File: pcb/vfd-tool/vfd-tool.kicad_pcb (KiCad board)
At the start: 2 copper layers, 167 parts, among them J1 Conn_ARM_SWD_TagConnect_TC203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, J2 USB_C_Receptacle_USB2.0, J3 Micro_SD_Card, J4 Conn_01x10, J5 Raspberry_Pi_2_3, J6 Conn_02x15_Odd_Even, J7 Conn_02x15_Odd_Even, J8 Conn_02x08_Odd_Even, J9 Conn_01x02_Socket, SW1 SW_Push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

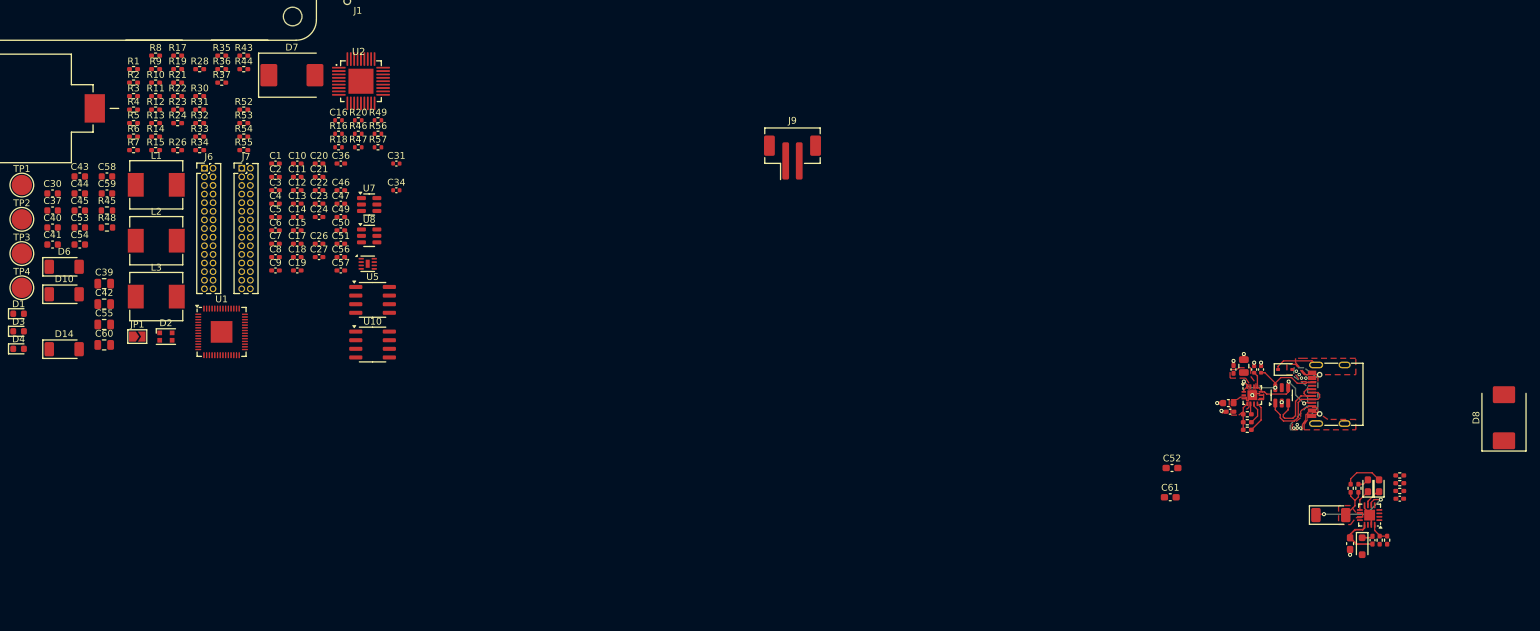
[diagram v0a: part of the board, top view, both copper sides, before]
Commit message: 3V3 + Charging + Fuel gauge PCB done
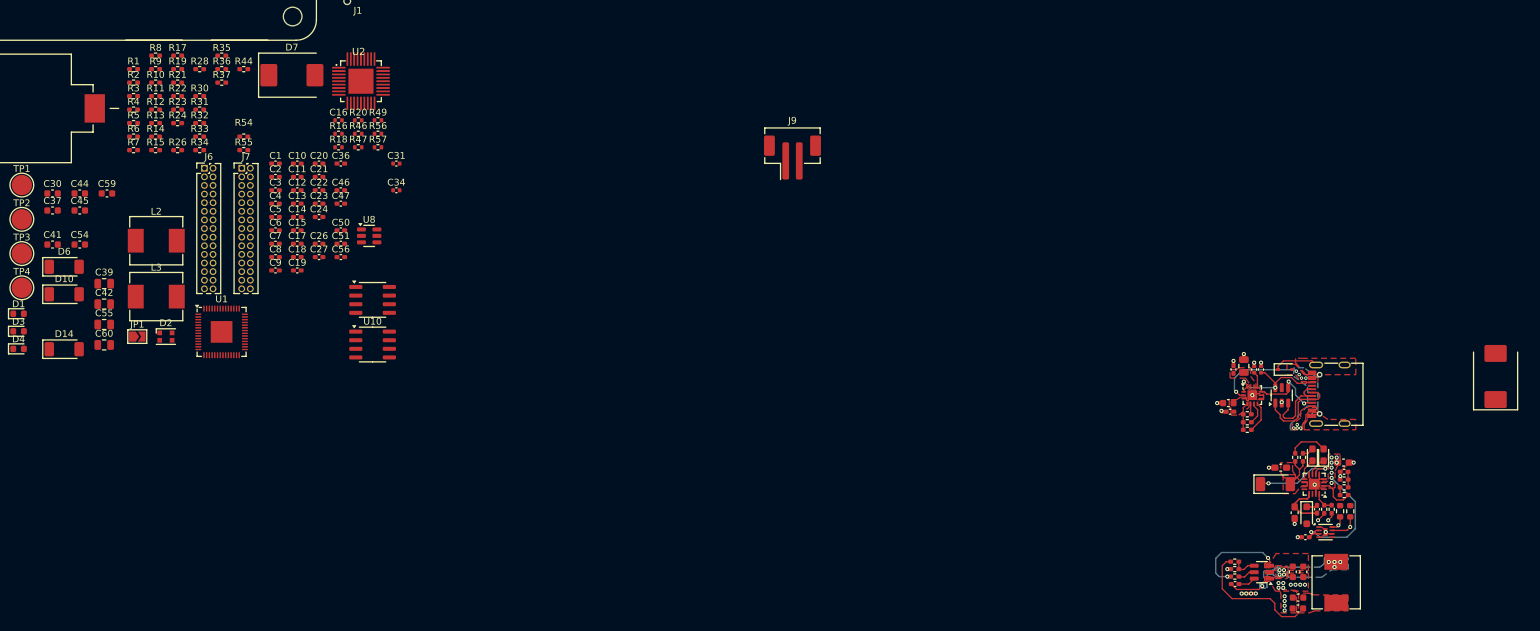
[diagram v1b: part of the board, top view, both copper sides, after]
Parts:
- moved C40 191.3 mm to (223.7, 123.0), turned to 90 degrees
- moved C43 188.1 mm to (222.1, 123.0), turned to -90 degrees
- moved R48 188.0 mm to (230.6, 114.1), turned to 90 degrees
- moved C53 187.7 mm to (222.9, 126.8)
- moved R45 187.1 mm to (229.1, 114.1), turned to 90 degrees
- moved C58 186.8 mm to (222.8, 128.4)
- moved L1 183.6 mm to (228.5, 124.6), turned to -90 degrees
- moved R43 165.1 mm to (213.6, 123.8)
- moved R52 160.6 mm to (213.5, 121.5)
- moved R53 160.2 mm to (213.5, 122.7), turned to 180 degrees
- moved C57 147.6 mm to (224.0, 117.9), turned to 180 degrees
- moved U9 146.7 mm to (226.9, 117.2)
- moved C49 142.5 mm to (213.6, 124.8)
- moved U7 142.3 mm to (217.6, 123.1), turned to 180 degrees
- moved C61 26.0 mm to (229.6, 106.9), turned to 180 degrees
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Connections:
- C40 pad 1: Net-(U7-GND) -> GND
- C41 pad 1: Net-(U8-GND) -> GND
- C43 pad 2: Net-(U7-GND) -> GND
- C44 pad 2: Net-(U8-GND) -> GND
- C57 pad 1: B+ -> 3V3
- U7 pad 1: Net-(U7-GND) -> GND
- U8 pad 1: Net-(U8-GND) -> GND
- U9 pad 2: B+ -> 3V3
- U9 pad 3: B+ -> 3V3
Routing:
- net 3V3: track 4.08 -> 43.8 mm, vias 0 -> 1
- net VSYS: track 12.5 -> 26.8 mm, vias 2 -> 4
- net GND: track 15.0 -> 28.2 mm, vias 9 -> 32
- net VBUS: track 0.00 -> 13.2 mm, vias 8 -> 9
- net B+: track 0.00 -> 5.33 mm, vias 0 -> 8
- net Net-(U7-SW): track 0.00 -> 5.11 mm, vias 0 -> 9
- net BATT_SCL: track 0.00 -> 4.39 mm, vias 0 -> 1
- net Net-(U7-VFB): track 0.00 -> 3.62 mm
- net Net-(U7-VBST): track 0.00 -> 2.58 mm
- net Net-(U7-EN): track 0.00 -> 2.58 mm
- net BATT_SDA: track 0.00 -> 2.39 mm, vias 0 -> 1
- net BATT_MONITOR: track 0.00 -> 2.30 mm
- net CHRG_CTRL_2: track 0.00 -> 1.40 mm, vias 0 -> 1
- net CHRG_CTRL_1: track 0.00 -> 1.23 mm, vias 0 -> 1
- net Net-(R38-Pad2): track 0.00 -> 1.14 mm
- added copper zone on F.Cu, net B+
- added copper zone on B.Cu, net Net-(U7-SW)
- added copper zone on F.Cu, net Net-(U7-SW)
- added copper zone on F.Cu, net VSYS

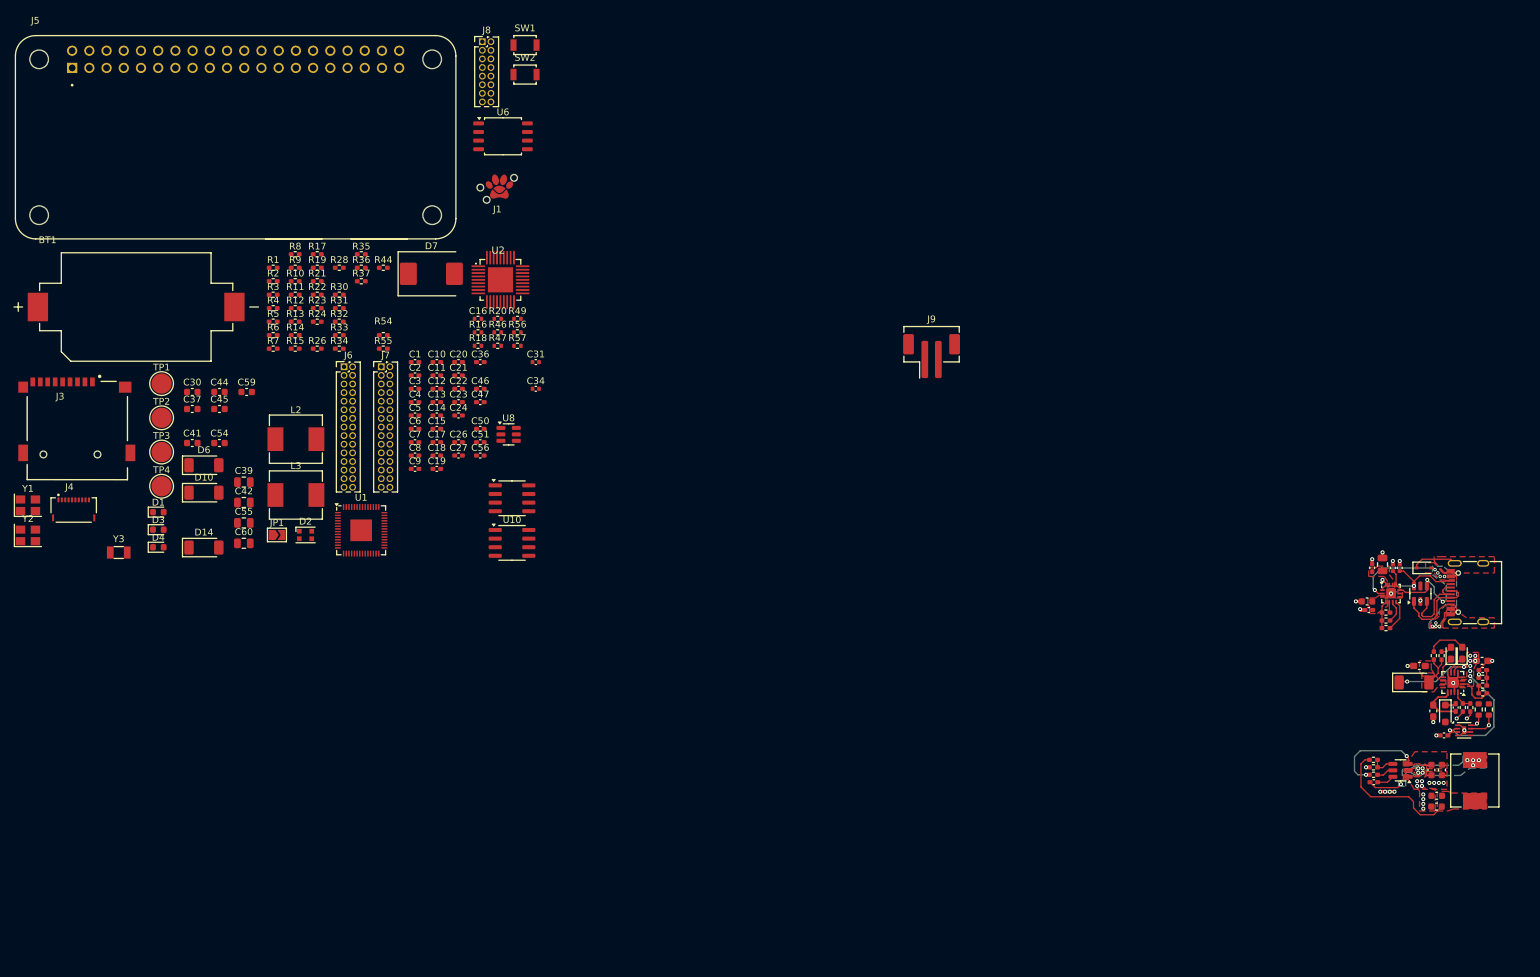
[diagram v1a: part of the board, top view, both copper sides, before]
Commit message: 5V & USB hub done
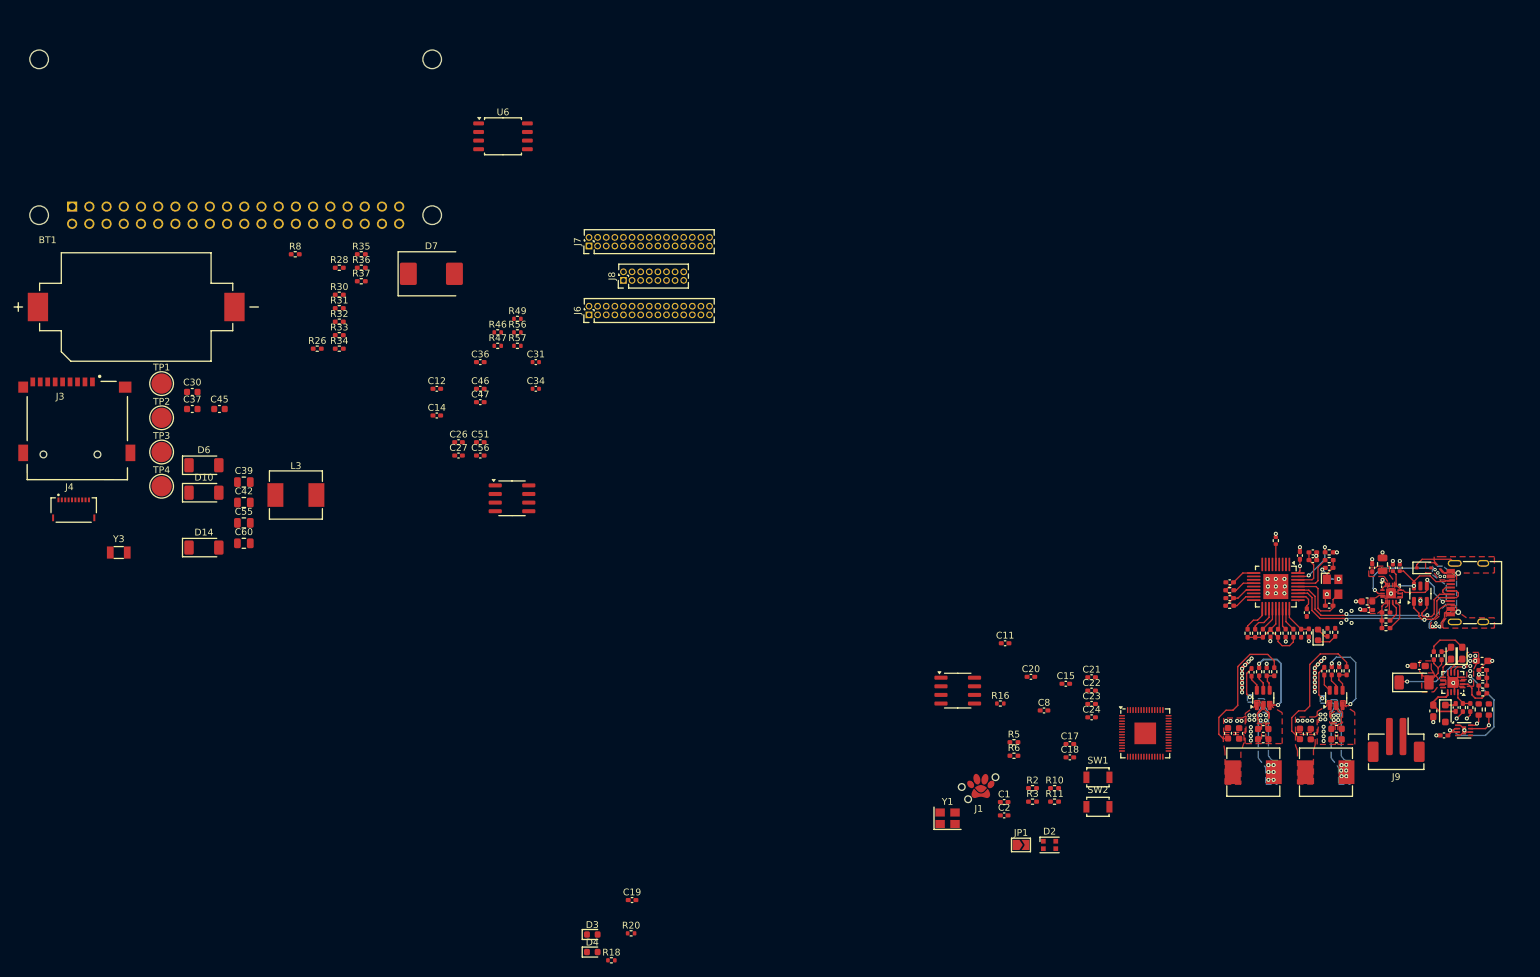
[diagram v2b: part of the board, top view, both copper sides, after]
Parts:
- added C62: 0.1uF, Capacitor_SMD:C_0402_1005Metric_Pad0.74x0.62mm_HandSolder, F.Cu at (202.7, 91.4)
- J5: moved to B.Cu
- moved Y2 192.7 mm to (207.5, 96.0), turned to -90 degrees
- moved D1 172.1 mm to (205.4, 103.1), turned to 90 degrees
- moved C41 164.0 mm to (197.3, 118.5)
- moved R4 162.8 mm to (206.8, 102.7), turned to 90 degrees
- moved R7 162.2 mm to (207.9, 102.7), turned to 90 degrees
- moved C44 161.9 mm to (197.3, 117.0), turned to 180 degrees
- moved R1 159.9 mm to (201.7, 102.9), turned to -90 degrees
- moved R9 158.6 mm to (207.0, 92.1)
- moved R13 156.5 mm to (204.0, 102.8), turned to -90 degrees
- moved R12 156.0 mm to (202.9, 102.9), turned to 90 degrees
- moved R14 155.9 mm to (207.0, 90.9)
- moved C59 154.9 mm to (193.7, 117.7), turned to -90 degrees
- moved C54 154.9 mm to (192.1, 117.6), turned to -90 degrees
- moved R17 152.4 mm to (199.5, 102.9), turned to -90 degrees
- moved R15 152.1 mm to (200.6, 102.9), turned to -90 degrees
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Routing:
- net 3V3: track 43.8 -> 77.9 mm, vias 1 -> 2
- net UP_D+: track 11.5 -> 33.4 mm, vias 0 -> 2
- net UP_D-: track 12.9 -> 34.4 mm, vias 0 -> 2
- net 5V: track 0.00 -> 20.9 mm
- net GND: track 28.2 -> 48.0 mm, vias 32 -> 82
- net Net-(U2-XTAL1): track 0.00 -> 10.9 mm
- net VSYS: track 26.8 -> 37.0 mm, vias 4 -> 6
- net Net-(U2-RBIAS): track 0.00 -> 7.58 mm, vias 0 -> 2
- net Net-(U2-XTAL2): track 0.00 -> 6.59 mm
- net Net-(U2-PLLFILT): track 0.00 -> 6.52 mm
- net Net-(U2-VBUS_DET): track 0.00 -> 4.89 mm
- net Net-(U8-SW): track 0.00 -> 4.71 mm, vias 0 -> 11
- net Net-(U2-OCS4): track 0.00 -> 4.32 mm
- net Net-(U2-OCS3): track 0.00 -> 4.28 mm
- net HUB_SDA: track 0.00 -> 3.60 mm
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- added copper zone on F.Cu, net 5V
- added copper zone on B.Cu, net Net-(U8-SW)
- added copper zone on F.Cu, net Net-(U8-SW)
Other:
- copper layers 2 -> 4

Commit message: Flash done and the majority of the RP2040 mcu done
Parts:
- J3: moved to B.Cu
- moved J3 204.1 mm to (226.2, 81.0)
- moved R8 181.4 mm to (231.8, 84.7)
- moved C37 170.4 mm to (209.2, 81.8)
- moved J8 158.5 mm to (248.4, 113.5)
- moved J6 158.5 mm to (243.3, 118.5)
- moved J7 158.5 mm to (243.3, 108.4)
- moved R35 154.6 mm to (212.1, 91.9), turned to -90 degrees
- moved R26 154.4 mm to (212.0, 66.4)
- moved R28 154.4 mm to (215.3, 54.5)
- moved R31 154.4 mm to (215.3, 60.5)
- moved R33 154.4 mm to (215.3, 64.5)
- moved R36 153.0 mm to (211.0, 91.9), turned to -90 degrees
- moved J5 141.9 mm to (174.5, 89.2)
- moved U6 140.3 mm to (213.8, 85.4), turned to 90 degrees
- moved C36 129.0 mm to (209.5, 80.5)
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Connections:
- net Net-(U1-USB_DM) renamed /2040_D-
- net Net-(U1-USB_DP) renamed /2040_D+
- U2 pad 6: EXTRA_USB4_D- -> EXTRA_USB3_D-
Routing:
- net RUN: track 0.00 -> 32.6 mm
- net 1V1: track 0.00 -> 20.4 mm
- net QSPI_SS: track 0.00 -> 18.3 mm, vias 0 -> 2
- net GND: track 48.0 -> 66.1 mm, vias 82 -> 92
- net 3V3: track 77.9 -> 95.4 mm, vias 2 -> 5
- net QSPI_SD3: track 0.00 -> 13.7 mm, vias 0 -> 2
- net UP_D+: track 33.4 -> 20.8 mm, vias 2 -> 0
- net UP_D-: track 34.4 -> 22.2 mm, vias 2 -> 0
- net QSPI_SCLK: track 0.00 -> 12.0 mm, vias 0 -> 2
- net QSPI__SD1: track 0.00 -> 11.4 mm, vias 0 -> 2
- net QSPI_SD0: track 0.00 -> 9.96 mm
- net QSPI_SD2: track 0.00 -> 9.34 mm
- net uSD_DAT2: track 0.00 -> 7.98 mm, vias 0 -> 1
- net Net-(U1-XIN): track 0.00 -> 6.81 mm
- net HUB_SUSP: track 2.01 -> 8.13 mm
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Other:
- board outline added: 95 x 50 mm

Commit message: 5V power done and general layour of of the PCB
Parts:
- added C63: 0.1uF, Capacitor_SMD:C_0402_1005Metric_Pad0.74x0.62mm_HandSolder, F.Cu at (225.7, 77.6)
- added G**: Paw-Connect_Silk_Full, Paw-Connect:Paw-Connect_Silk_Full, F.Cu at (233.3, 97.2)
- BT1, C30, J4, R26, R28, R30, R31, R33: moved to B.Cu
- C47, C51, C56: footprint Capacitor_SMD:C_0402_1005Metric_Pad0.74x0.62mm_HandSolder -> Capacitor_SMD:C_0402_1005Metric
- moved J4 193.7 mm to (213.1, 113.5), turned to 180 degrees
- moved C30 186.7 mm to (224.5, 90.6), turned to -90 degrees
- moved TP2 166.9 mm to (200.2, 49.5), turned to 180 degrees
- moved R30 166.4 mm to (222.7, 91.8), turned to 90 degrees
- moved TP1 165.9 mm to (200.2, 54.5), turned to 180 degrees
- moved TP4 163.6 mm to (195.2, 49.5), turned to 180 degrees
- moved TP3 162.0 mm to (195.2, 54.5), turned to 180 degrees
- moved D4 155.7 mm to (234.9, 75.2), turned to 180 degrees
- moved R20 148.3 mm to (234.5, 76.6), turned to 180 degrees
- moved C19 145.2 mm to (235.1, 79.6)
- moved D14 143.9 mm to (184.3, 77.9), turned to -90 degrees
- moved D7 143.1 mm to (204.4, 110.0)
- moved BT1 142.1 mm to (160.2, 113.6)
- moved D3 137.2 mm to (231.3, 113.9), turned to -90 degrees
- moved R18 136.9 mm to (232.7, 113.5), turned to 90 degrees
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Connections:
- C30 pad 2: Net-(J3-VDD) -> GND
- J3 pad 4: Net-(J3-VDD) -> 3V3
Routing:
- net HUB_SDA: track 3.60 -> 54.3 mm, vias 0 -> 4
- net HUB_SCL: track 3.10 -> 50.2 mm, vias 0 -> 4
- net PD_SDA: track 4.66 -> 44.3 mm, vias 0 -> 2
- net BATT_SCL: track 7.24 -> 45.4 mm, vias 1 -> 2
- net BATT_SDA: track 4.54 -> 42.5 mm, vias 1 -> 2
- net PD_SCL: track 3.33 -> 31.7 mm, vias 0 -> 4
- net SWD_RP2040: track 0.00 -> 26.6 mm, vias 0 -> 2
- net SWCLK_RP2040: track 0.49 -> 26.8 mm, vias 1 -> 2
- net UP_D+: track 20.8 -> 47.0 mm, vias 0 -> 2
- net UP_D-: track 22.2 -> 47.9 mm, vias 0 -> 2
- net 3V3: track 95.4 -> 120.0 mm, vias 5 -> 6
- net ONEWIRE_DETECT: track 0.00 -> 19.8 mm
- net Net-(U10-BOOT): track 0.00 -> 14.7 mm
- net LED: track 0.00 -> 14.2 mm, vias 0 -> 2
- net Net-(D6-K): track 0.00 -> 13.4 mm
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- added copper zone on B.Cu, net B+
- added copper zone on F.Cu, net EXT_PWR
- added copper zone on F.Cu, net Net-(D10-A)
- added copper zone on F.Cu, net Net-(D14-A)
